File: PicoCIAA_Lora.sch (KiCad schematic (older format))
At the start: 5 parts

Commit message: Primer avance del esquema
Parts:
- removed C?: 0.1uF 10V, symbol C
- removed Conn? (x2): Conn_Pico, symbol Conn_Pico
- added C1: 15nF, symbol C
- added C2: 0.1uF, symbol C
- added P1: IO1, symbol CONN_02X10
- added R1: 1K, symbol R
- added SW1: RESET, symbol SW_Push
- gave numbers to parts that had none: 2
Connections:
- net labels added: DIO0, DIO1, DIO2, DIO3, DIO4, DIO5, MISO, MOSI, RESET, SCK, nCS
- wire segments 2 -> 37
- no-connect marks 0 -> 9
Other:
- moved on the sheet: U2

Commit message: Actualizando esquemático
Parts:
- removed C1: 15nF, symbol C
- removed R1: 1K, symbol R
- removed SW1: RESET, symbol SW_Push
- C2: value 0.1uF -> 0.1uF 10v; Digikey# (none) -> 399-3520-1-ND; Manf (none) -> KEMET; Manf# (none) -> C0402C104K8RACTU
- U1: Digikey# (none) -> RFM95W-915S2-ND; Fieldname (none) -> Value; Manf (none) -> HopeRF; Manf# (none) -> RFM95W-915S2
- U2: Digikey# (none) -> WM5534-ND; Fieldname (none) -> Value; Manf (none) -> Molex; Manf# (none) -> 0732511150
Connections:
- net RESET: no longer names the net of U1.6 (RESET)
- no-connect marks 9 -> 11
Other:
- note added: "Uso del conector P6 de la PicoCIAA"
- moved on the sheet: C2, P1, U1, U2

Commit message: Actualizando esquema
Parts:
- added P3: PWR, footprints:Pin_Header_Straight_1x02_Pitch2.00mm, symbol CONN_01X02
- added P4, P5: MOUNTING_HOLE, footprints:PIN_ARRAY_1, symbol CONN_01X01
- added P8: IO3, footprints:Pin_Header_Straight_2x05_Pitch2.00mm, symbol CONN_02X05
- C2: footprint (none) -> Capacitors_SMD:C_0402
- P6: renamed from P1; footprint (none) -> footprints:Pin_Header_Straight_2x10_Pitch2.00mm
- U1: footprint (none) -> footprints:RFM95W
- U2: footprint (none) -> footprints:SMA_EDGE
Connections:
- net +3V3: now also P3.1 (P1)
- net GND: now also P3.2 (P2), P4.1 (P1), P5.1 (P1)
- no-connect marks 11 -> 21
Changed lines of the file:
@@
 F 0 "U1" H 5400 2550 60  0000 C CNN
 F 1 "RFM92/95/96/97/98" H 5350 3500 60  0000 C CNN
-F 2 "" H 5550 3150 60  0001 C CNN
+F 2 "footprints:RFM95W" H 5550 3150 60  0001 C CNN
 F 3 "" H 5550 3150 60  0001 C CNN
 F 4 "HopeRF" H 5350 2950 60  0001 C CNN "Manf"
@@
 F 0 "U2" H 5850 3900 60  0000 C CNN
 F 1 "EDGE_SMA" H 5800 4250 60  0000 C CNN
-F 2 "" H 5800 4050 60  0001 C CNN
+F 2 "footprints:SMA_EDGE" H 5800 4050 60  0001 C CNN
 F 3 "" H 5800 4050 60  0001 C CNN
 F 4 "Molex" H 5800 4050 60  0001 C CNN "Manf"
@@
 DIO2
 $Comp
-L CONN_02X10 P1
+L CONN_02X10 P6
 U 1 1 592B383E
 P 3300 3050
-F 0 "P1" H 3300 3600 50  0000 C CNN
+F 0 "P6" H 3300 3600 50  0000 C CNN
 F 1 "IO1" V 3300 3050 50  0000 C CNN
-F 2 "" H 3300 1850 50  0000 C CNN
+F 2 "footprints:Pin_Header_Straight_2x10_Pitch2.00mm" H 3300 1850 50  0001 C CNN
 F 3 "" H 3300 1850 50  0000 C CNN
 F 4 "Value" H 3300 3050 60  0001 C CNN "Fieldname"
@@
 F 0 "C2" H 7075 3700 50  0000 L CNN
 F 1 "0.1uF 10v" H 7075 3500 50  0000 L CNN
-F 2 "" H 7088 3450 50  0000 C CNN
+F 2 "Capacitors_SMD:C_0402" H 7088 3450 50  0001 C CNN
 F 3 "" H 7050 3600 50  0000 C CNN
 F 4 "KEMET" H 7050 3600 60  0001 C CNN "Manf"
@@
 Wire Notes Line
 	2450 2250 2450 2050
+$Comp
+L CONN_01X01 P4
+U 1 1 59452957
+P 8200 2500
+F 0 "P4" H 8200 2600 50  0000 C CNN
+F 1 "MOUNTING_HOLE" H 8350 2400 50  0000 C CNN
+F 2 "footprints:PIN_ARRAY_1" H 8200 2500 50  0001 C CNN
+F 3 "" H 8200 2500 50  0000 C CNN
+F 4 "Value" H 8200 2500 60  0001 C CNN "Fieldname"
+	1    8200 2500
+	1    0    0    -1
+$EndComp
+$Comp
+L CONN_01X01 P5
+U 1 1 5945298A
+P 8200 2850
+F 0 "P5" H 8200 2950 50  0000 C CNN
+F 1 "MOUNTING_HOLE" H 8350 2750 50  0000 C CNN
+F 2 "footprints:PIN_ARRAY_1" H 8200 2850 50  0001 C CNN
+F 3 "" H 8200 2850 50  0000 C CNN
+	1    8200 2850
+	1    0    0    -1
+$EndComp
+Wire Wire Line
+	8000 2500 8000 3100
+$Comp
+L GND #PWR012
+U 1 1 59452AC9
+P 8000 3100
+F 0 "#PWR012" H 8000 2850 50  0001 C CNN
+F 1 "GND" H 8000 2950 50  0000 C CNN
+F 2 "" H 8000 3100 50  0000 C CNN
+F 3 "" H 8000 3100 50  0000 C CNN
+	1    8000 3100
+	1    0    0    -1
+$EndComp
+Connection ~ 8000 2850
+$Comp
+L CONN_01X02 P3
+U 1 1 59454385
+P 8200 3950
+F 0 "P3" H 8200 4100 50  0000 C CNN
+F 1 "PWR" V 8300 3950 50  0000 C CNN
+F 2 "footprints:Pin_Header_Straight_1x02_Pitch2.00mm" H 8200 3950 50  0001 C CNN
+F 3 "" H 8200 3950 50  0000 C CNN
+F 4 "Value" H 8200 3950 60  0001 C CNN "Fieldname"
+	1    8200 3950
+	1    0    0    -1
+$EndComp
+$Comp
+L +3.3V #PWR013
+U 1 1 59454C80
+P 8000 3700
+F 0 "#PWR013" H 8000 3550 50  0001 C CNN
+F 1 "+3.3V" H 8000 3840 50  0000 C CNN
+F 2 "" H 8000 3700 50  0000 C CNN
+F 3 "" H 8000 3700 50  0000 C CNN
+	1    8000 3700
+	1    0    0    -1
+$EndComp
+$Comp
+L GND #PWR014
+U 1 1 59454CA9
+P 8000 4200
+F 0 "#PWR014" H 8000 3950 50  0001 C CNN
+F 1 "GND" H 8000 4050 50  0000 C CNN
+F 2 "" H 8000 4200 50  0000 C CNN
+F 3 "" H 8000 4200 50  0000 C CNN
+	1    8000 4200
+	1    0    0    -1
+$EndComp
+Wire Wire Line
+	8000 3700 8000 3900
+Wire Wire Line
+	8000 4000 8000 4200
+$Comp
+L CONN_02X05 P8
+U 1 1 59454B63
+P 3250 4200
+F 0 "P8" H 3250 4500 50  0000 C CNN
+F 1 "IO3" V 3250 4200 50  0000 C CNN
+F 2 "footprints:Pin_Header_Straight_2x05_Pitch2.00mm" H 3250 3000 50  0001 C CNN
+F 3 "" H 3250 3000 50  0000 C CNN
+	1    3250 4200
+	1    0    0    -1
+$EndComp
+NoConn ~ 3000 4000
+NoConn ~ 3000 4100
+NoConn ~ 3000 4200
+NoConn ~ 3000 4300
+NoConn ~ 3000 4400
+NoConn ~ 3500 4000
+NoConn ~ 3500 4100
+NoConn ~ 3500 4200
+NoConn ~ 3500 4300
+NoConn ~ 3500 4400
 $EndSCHEMATC

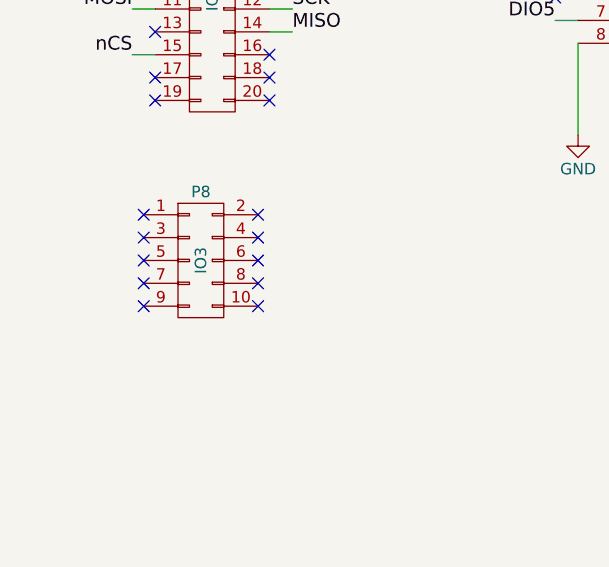
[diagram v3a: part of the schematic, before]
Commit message: PCB: Delimitando con bordes
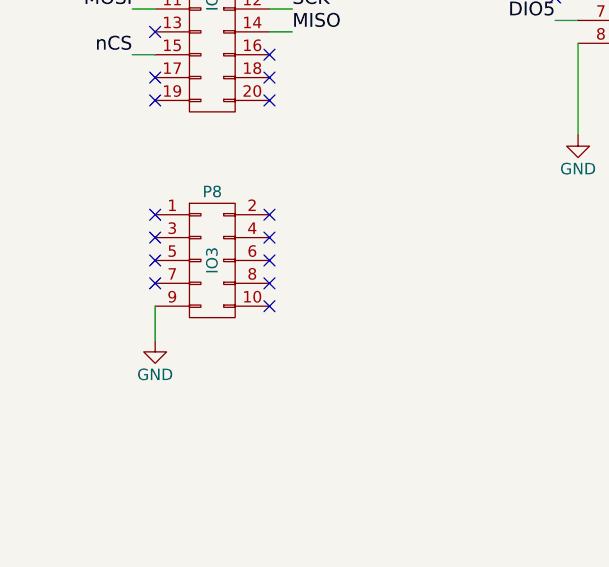
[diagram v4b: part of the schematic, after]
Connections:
- net GND: now also P8.9 (P9)
- no-connect marks 21 -> 20
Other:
- moved on the sheet: P8
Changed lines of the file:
@@
 L CONN_02X05 P8
 U 1 1 59454B63
-P 3250 4200
-F 0 "P8" H 3250 4500 50  0000 C CNN
-F 1 "IO3" V 3250 4200 50  0000 C CNN
-F 2 "footprints:Pin_Header_Straight_2x05_Pitch2.00mm" H 3250 3000 50  0001 C CNN
-F 3 "" H 3250 3000 50  0000 C CNN
-	1    3250 4200
+P 3300 4200
+F 0 "P8" H 3300 4500 50  0000 C CNN
+F 1 "IO3" V 3300 4200 50  0000 C CNN
+F 2 "footprints:Pin_Header_Straight_2x05_Pitch2.00mm" H 3300 3000 50  0001 C CNN
+F 3 "" H 3300 3000 50  0000 C CNN
+	1    3300 4200
 	1    0    0    -1
 $EndComp
-NoConn ~ 3000 4000
-NoConn ~ 3000 4100
-NoConn ~ 3000 4200
-NoConn ~ 3000 4300
-NoConn ~ 3000 4400
-NoConn ~ 3500 4000
-NoConn ~ 3500 4100
-NoConn ~ 3500 4200
-NoConn ~ 3500 4300
-NoConn ~ 3500 4400
+NoConn ~ 3050 4000
+NoConn ~ 3050 4100
+NoConn ~ 3050 4200
+NoConn ~ 3050 4300
+NoConn ~ 3550 4000
+NoConn ~ 3550 4100
+NoConn ~ 3550 4200
+NoConn ~ 3550 4300
+NoConn ~ 3550 4400
+$Comp
+L GND #PWR?
+U 1 1 594DB5B8
+P 3050 4550
+F 0 "#PWR?" H 3050 4300 50  0001 C CNN
+F 1 "GND" H 3050 4400 50  0000 C CNN
+F 2 "" H 3050 4550 50  0000 C CNN
+F 3 "" H 3050 4550 50  0000 C CNN
+	1    3050 4550
+	1    0    0    -1
+$EndComp
+Wire Wire Line
+	3050 4400 3050 4550
 $EndSCHEMATC

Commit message: SCH: Actualizando esquematico
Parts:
- U1: value RFM92/95/96/97/98 -> RFM95
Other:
- moved on the sheet: P3
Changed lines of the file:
@@
 Date "2017-06-10"
 Rev ""
-Comp "Author: Elías Alejandro Año Mendoza"
-Comment1 "CESE 4ta cohorte"
+Comp "Autor: Elías Alejandro Año Mendoza"
+Comment1 "Revisor: "
 Comment2 "Licencia: Ver en 'doc/LICENCIA.txt'"
-Comment3 ""
-Comment4 ""
+Comment3 "Asignatura: Diseño de Circuitos Impresos"
+Comment4 "CESE - FIUBA"
 $EndDescr
 $Comp
@@
 P 5350 2950
 F 0 "U1" H 5400 2550 60  0000 C CNN
-F 1 "RFM92/95/96/97/98" H 5350 3500 60  0000 C CNN
+F 1 "RFM95" H 5350 3500 60  0000 C CNN
 F 2 "footprints:RFM95W" H 5550 3150 60  0001 C CNN
 F 3 "" H 5550 3150 60  0001 C CNN
@@
 NoConn ~ 3550 3500
 NoConn ~ 3550 3400
-$Comp
-L PWR_FLAG #FLG08
-U 1 1 592E0F8A
-P 5950 2000
-F 0 "#FLG08" H 5950 2095 50  0001 C CNN
-F 1 "PWR_FLAG" H 5950 2180 50  0000 C CNN
-F 2 "" H 5950 2000 50  0000 C CNN
-F 3 "" H 5950 2000 50  0000 C CNN
-	1    5950 2000
-	1    0    0    -1
-$EndComp
-$Comp
-L +3.3V #PWR09
-U 1 1 592E1591
-P 6400 2000
-F 0 "#PWR09" H 6400 1850 50  0001 C CNN
-F 1 "+3.3V" H 6400 2140 50  0000 C CNN
-F 2 "" H 6400 2000 50  0000 C CNN
-F 3 "" H 6400 2000 50  0000 C CNN
-	1    6400 2000
-	1    0    0    -1
-$EndComp
-$Comp
-L PWR_FLAG #FLG010
-U 1 1 592E1605
-P 7000 2050
-F 0 "#FLG010" H 7000 2145 50  0001 C CNN
-F 1 "PWR_FLAG" H 7000 2230 50  0000 C CNN
-F 2 "" H 7000 2050 50  0000 C CNN
-F 3 "" H 7000 2050 50  0000 C CNN
-	1    7000 2050
-	1    0    0    -1
-$EndComp
-$Comp
-L GND #PWR011
-U 1 1 592E17A6
-P 7300 2050
-F 0 "#PWR011" H 7300 1800 50  0001 C CNN
-F 1 "GND" H 7300 1900 50  0000 C CNN
-F 2 "" H 7300 2050 50  0000 C CNN
-F 3 "" H 7300 2050 50  0000 C CNN
-	1    7300 2050
-	1    0    0    -1
-$EndComp
 NoConn ~ 4800 3050
 Text Notes 2500 2200 0    60   ~ 0
@@
 Wire Wire Line
 	3050 2800 2950 2800
-Wire Wire Line
-	6400 2000 6400 2200
-Wire Wire Line
-	6400 2200 5950 2200
-Wire Wire Line
-	5950 2200 5950 2000
-Wire Wire Line
-	7000 2050 7300 2050
 Wire Wire Line
 	5850 2850 7050 2850
@@
 	8000 2500 8000 3100
 $Comp
-L GND #PWR012
+L GND #PWR08
 U 1 1 59452AC9
 P 8000 3100
-F 0 "#PWR012" H 8000 2850 50  0001 C CNN
+F 0 "#PWR08" H 8000 2850 50  0001 C CNN
 F 1 "GND" H 8000 2950 50  0000 C CNN
 F 2 "" H 8000 3100 50  0000 C CNN
@@
 L CONN_01X02 P3
 U 1 1 59454385
-P 8200 3950
-F 0 "P3" H 8200 4100 50  0000 C CNN
-F 1 "PWR" V 8300 3950 50  0000 C CNN
-F 2 "footprints:Pin_Header_Straight_1x02_Pitch2.00mm" H 8200 3950 50  0001 C CNN
-F 3 "" H 8200 3950 50  0000 C CNN
-F 4 "Value" H 8200 3950 60  0001 C CNN "Fieldname"
-	1    8200 3950
-	1    0    0    -1
-$EndComp
-$Comp
-L +3.3V #PWR013
+P 8800 3900
+F 0 "P3" H 8800 4050 50  0000 C CNN
+F 1 "PWR" V 8900 3900 50  0000 C CNN
+F 2 "footprints:Pin_Header_Straight_1x02_Pitch2.00mm" H 8800 3900 50  0001 C CNN
+F 3 "" H 8800 3900 50  0000 C CNN
+F 4 "Value" H 8800 3900 60  0001 C CNN "Fieldname"
+	1    8800 3900
+	1    0    0    -1
+$EndComp
+$Comp
+L +3.3V #PWR09
 U 1 1 59454C80
-P 8000 3700
-F 0 "#PWR013" H 8000 3550 50  0001 C CNN
-F 1 "+3.3V" H 8000 3840 50  0000 C CNN
-F 2 "" H 8000 3700 50  0000 C CNN
-F 3 "" H 8000 3700 50  0000 C CNN
-	1    8000 3700
-	1    0    0    -1
-$EndComp
-$Comp
-L GND #PWR014
+P 8600 3650
+F 0 "#PWR09" H 8600 3500 50  0001 C CNN
+F 1 "+3.3V" H 8600 3790 50  0000 C CNN
+F 2 "" H 8600 3650 50  0000 C CNN
+F 3 "" H 8600 3650 50  0000 C CNN
+	1    8600 3650
+	1    0    0    -1
+$EndComp
+$Comp
+L GND #PWR010
 U 1 1 59454CA9
-P 8000 4200
-F 0 "#PWR014" H 8000 3950 50  0001 C CNN
-F 1 "GND" H 8000 4050 50  0000 C CNN
-F 2 "" H 8000 4200 50  0000 C CNN
-F 3 "" H 8000 4200 50  0000 C CNN
-	1    8000 4200
-	1    0    0    -1
-$EndComp
-Wire Wire Line
-	8000 3700 8000 3900
-Wire Wire Line
-	8000 4000 8000 4200
+P 8600 4150
+F 0 "#PWR010" H 8600 3900 50  0001 C CNN
+F 1 "GND" H 8600 4000 50  0000 C CNN
+F 2 "" H 8600 4150 50  0000 C CNN
+F 3 "" H 8600 4150 50  0000 C CNN
+	1    8600 4150
+	1    0    0    -1
+$EndComp
+Wire Wire Line
+	8600 3650 8600 3850
+Wire Wire Line
+	8600 3950 8600 4150
 $Comp
 L CONN_02X05 P8
@@
 NoConn ~ 3550 4400
 $Comp
-L GND #PWR?
+L GND #PWR011
 U 1 1 594DB5B8
 P 3050 4550
-F 0 "#PWR?" H 3050 4300 50  0001 C CNN
+F 0 "#PWR011" H 3050 4300 50  0001 C CNN
 F 1 "GND" H 3050 4400 50  0000 C CNN
 F 2 "" H 3050 4550 50  0000 C CNN
@@
 Wire Wire Line
 	3050 4400 3050 4550
+$Comp
+L PWR_FLAG #FLG?
+U 1 1 5960DE94
+P 8150 3700
+F 0 "#FLG?" H 8150 3795 50  0001 C CNN
+F 1 "PWR_FLAG" H 8150 3880 50  0000 C CNN
+F 2 "" H 8150 3700 50  0000 C CNN
+F 3 "" H 8150 3700 50  0000 C CNN
+	1    8150 3700
+	1    0    0    -1
+$EndComp
+$Comp
+L PWR_FLAG #FLG?
+U 1 1 5960DEB8
+P 8150 4100
+F 0 "#FLG?" H 8150 4195 50  0001 C CNN
+F 1 "PWR_FLAG" H 8150 4280 50  0000 C CNN
+F 2 "" H 8150 4100 50  0000 C CNN
+F 3 "" H 8150 4100 50  0000 C CNN
+	1    8150 4100
+	1    0    0    -1
+$EndComp
+Wire Wire Line
+	8150 3700 8600 3700
+Connection ~ 8600 3700
+Wire Wire Line
+	8150 4100 8600 4100
+Connection ~ 8600 4100
 $EndSCHEMATC

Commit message: SCH: Agregando campo DigiKey
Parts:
- P3: Digikey# (none) -> SAM1247-02-ND; Manf (none) -> Samtec Inc.; Manf# (none) -> SQT-102-01-L-S
- P6: Digikey# (none) -> 952-1361-5-ND; Manf (none) -> Harwin Inc.; Manf# (none) -> M22-7141042
- P8: Digikey# (none) -> 952-1359-5-ND; Fieldname (none) -> Value; Manf (none) -> Harwin Inc.; Manf# (none) -> M22-7140542
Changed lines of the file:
@@
 EESchema Schematic File Version 2
-LIBS:74xgxx
-LIBS:74xx
-LIBS:ac-dc
-LIBS:actel
-LIBS:adc-dac
-LIBS:allegro
-LIBS:Altera
-LIBS:analog_devices
-LIBS:analog_switches
-LIBS:atmel
-LIBS:audio
-LIBS:battery_management
-LIBS:bbd
-LIBS:brooktre
-LIBS:cmos4000
-LIBS:cmos_ieee
-LIBS:conn
-LIBS:contrib
-LIBS:cypress
-LIBS:dc-dc
-LIBS:device
-LIBS:digital-audio
-LIBS:diode
-LIBS:display
-LIBS:dsp
-LIBS:elec-unifil
-LIBS:ESD_Protection
-LIBS:ftdi
-LIBS:gennum
-LIBS:graphic
-LIBS:hc11
-LIBS:intel
-LIBS:interface
-LIBS:ir
-LIBS:Lattice
-LIBS:linear
-LIBS:logo
-LIBS:maxim
-LIBS:mechanical
-LIBS:memory
-LIBS:microchip_dspic33dsc
-LIBS:microchip
-LIBS:microchip_pic10mcu
-LIBS:microchip_pic12mcu
-LIBS:microchip_pic16mcu
-LIBS:microchip_pic18mcu
-LIBS:microchip_pic32mcu
-LIBS:microcontrollers
-LIBS:motor_drivers
-LIBS:motorola
-LIBS:motors
-LIBS:msp430
-LIBS:nordicsemi
-LIBS:nxp_armmcu
-LIBS:onsemi
-LIBS:opto
-LIBS:Oscillators
-LIBS:philips
-LIBS:powerint
-LIBS:power
-LIBS:Power_Management
-LIBS:pspice
-LIBS:references
-LIBS:regul
-LIBS:relays
-LIBS:rfcom
-LIBS:sensors
-LIBS:silabs
-LIBS:siliconi
-LIBS:sim5320_KICAD_PART
-LIBS:stm32
-LIBS:supertex
-LIBS:switches
-LIBS:texas
-LIBS:transf
-LIBS:transistors
-LIBS:ttl_ieee
-LIBS:valves
-LIBS:video
-LIBS:wiznet
-LIBS:Worldsemi
-LIBS:Xicor
-LIBS:xilinx
-LIBS:zetex
-LIBS:Zilog
 LIBS:PicoLora
+LIBS:SMA
 LIBS:PicoCIAA_Lora-cache
 EELAYER 25 0
@@
 F 2 "footprints:Pin_Header_Straight_2x10_Pitch2.00mm" H 3300 1850 50  0001 C CNN
 F 3 "" H 3300 1850 50  0000 C CNN
-F 4 "Value" H 3300 3050 60  0001 C CNN "Fieldname"
+F 4 "Harwin Inc." H 3300 3050 60  0001 C CNN "Manf"
+F 5 "M22-7141042" H 3300 3050 60  0001 C CNN "Manf#"
+F 6 "952-1361-5-ND" H 3300 3050 60  0001 C CNN "Digikey#"
+F 7 "Value" H 3300 3050 60  0001 C CNN "Fieldname"
 	1    3300 3050
 	1    0    0    -1
@@
 F 2 "footprints:Pin_Header_Straight_1x02_Pitch2.00mm" H 8800 3900 50  0001 C CNN
 F 3 "" H 8800 3900 50  0000 C CNN
-F 4 "Value" H 8800 3900 60  0001 C CNN "Fieldname"
+F 4 "Samtec Inc." H 8800 3900 60  0001 C CNN "Manf"
+F 5 "SQT-102-01-L-S" H 8800 3900 60  0001 C CNN "Manf#"
+F 6 "SAM1247-02-ND" H 8800 3900 60  0001 C CNN "Digikey#"
+F 7 "Value" H 8800 3900 60  0001 C CNN "Fieldname"
 	1    8800 3900
 	1    0    0    -1
@@
 F 2 "footprints:Pin_Header_Straight_2x05_Pitch2.00mm" H 3300 3000 50  0001 C CNN
 F 3 "" H 3300 3000 50  0000 C CNN
+F 4 "Harwin Inc." H 3300 4200 60  0001 C CNN "Manf"
+F 5 "M22-7140542" H 3300 4200 60  0001 C CNN "Manf#"
+F 6 "952-1359-5-ND" H 3300 4200 60  0001 C CNN "Digikey#"
+F 7 "Value" H 3300 4200 60  0001 C CNN "Fieldname"
 	1    3300 4200
 	1    0    0    -1
